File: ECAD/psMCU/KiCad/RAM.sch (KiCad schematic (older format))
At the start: 34 parts, among them U54 SN74LVC1G04DCK, U55 SN74LVC1G08DCK, U56 SN74LVC1G08DCK, U57 SN74LVC1G08DCK, U58 SN74LVC1G32DCK, U59 SN74LVC1G175DCK, U60 SN74LVC1G04DCK, U61 SN74LVC1G175DCK, U62 SN74LVC1G126DCK, U63 IS62C256AL-45T, U64 SN74LVC1G04DCK, U65 SN74LVC1G04DCK, U66 SN74HC245PW, U67 SN74HC245PW

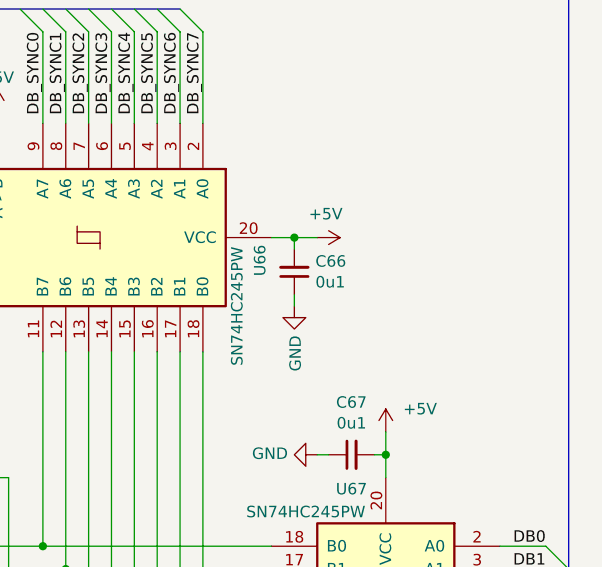
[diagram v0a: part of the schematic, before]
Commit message: Sch: Removed Regulator, Added extra spread bulk C
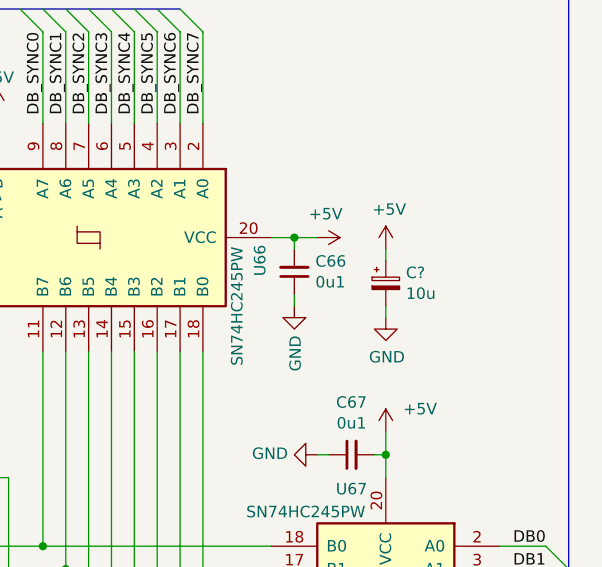
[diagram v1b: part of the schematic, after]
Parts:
- added C?: 10u, symbol Device:CP_Small
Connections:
- net +5V: now also C?.1
- net GND: now also C?.2
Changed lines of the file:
@@
 F9 "Latch_A" I L 3800 1600 50
 $EndSheet
+$Comp
+L Device:CP_Small C?
+U 1 1 625715F0
+P 9950 2000
+AR Path="/62043340/625715F0" Ref="C?"  Part="1"
+AR Path="/5FD6B215/625715F0" Ref="C?"  Part="1"
+F 0 "C?" H 10038 2046 50  0000 L CNN
+F 1 "10u" H 10038 1955 50  0000 L CNN
+F 2 "" H 9950 2000 50  0001 C CNN
+F 3 "~" H 9950 2000 50  0001 C CNN
+	1    9950 2000
+	1    0    0    -1
+$EndComp
+$Comp
+L power:GND #PWR?
+U 1 1 625715F6
+P 9950 2150
+AR Path="/625715F6" Ref="#PWR?"  Part="1"
+AR Path="/62043340/625715F6" Ref="#PWR?"  Part="1"
+AR Path="/5FD6B215/625715F6" Ref="#PWR?"  Part="1"
+F 0 "#PWR?" H 9950 1900 50  0001 C CNN
+F 1 "GND" H 9955 1977 50  0000 C CNN
+F 2 "" H 9950 2150 50  0001 C CNN
+F 3 "" H 9950 2150 50  0001 C CNN
+	1    9950 2150
+	1    0    0    -1
+$EndComp
+Wire Wire Line
+	9950 2150 9950 2100
+Wire Wire Line
+	9950 1850 9950 1900
+$Comp
+L power:+5V #PWR?
+U 1 1 625715FE
+P 9950 1850
+AR Path="/625715FE" Ref="#PWR?"  Part="1"
+AR Path="/62043340/625715FE" Ref="#PWR?"  Part="1"
+AR Path="/5FD6B215/625715FE" Ref="#PWR?"  Part="1"
+F 0 "#PWR?" H 9950 1700 50  0001 C CNN
+F 1 "+5V" H 9965 2023 50  0000 C CNN
+F 2 "" H 9950 1850 50  0001 C CNN
+F 3 "" H 9950 1850 50  0001 C CNN
+	1    9950 1850
+	1    0    0    -1
+$EndComp
 Wire Bus Line
 	5850 3350 5850 4000

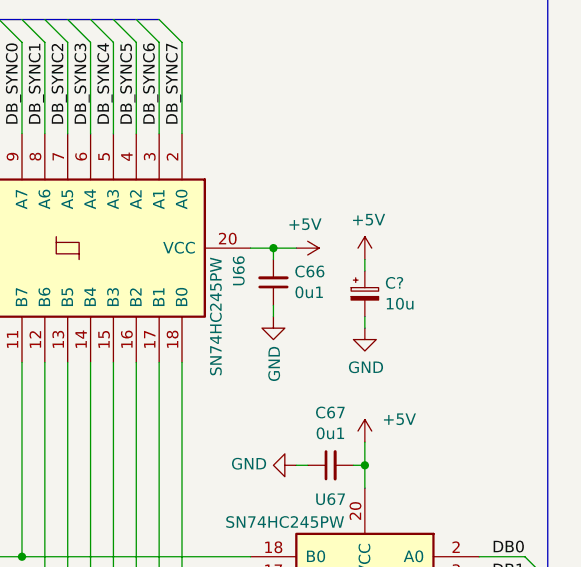
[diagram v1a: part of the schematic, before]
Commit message: Sch: Reworked Peripheral Interface (Buffers)
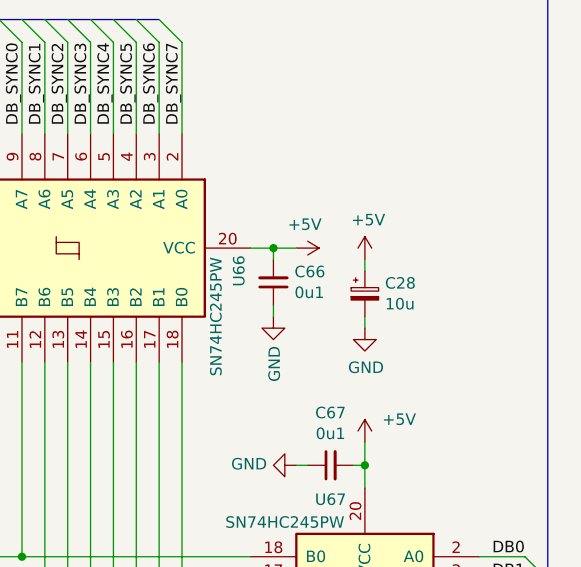
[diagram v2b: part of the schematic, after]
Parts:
- gave numbers to parts that had none: 1
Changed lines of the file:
@@
 $Descr A4 11693 8268
 encoding utf-8
-Sheet 34 97
+Sheet 34 96
 Title "psMCU"
 Date "2022-02-13"
@@
 AR Path="/62043340/625715F0" Ref="C?"  Part="1"
 AR Path="/5FD6B215/625715F0" Ref="C?"  Part="1"
-F 0 "C?" H 10038 2046 50  0000 L CNN
+AR Path="/5ED3C49A/625715F0" Ref="C28"  Part="1"
+F 0 "C28" H 10038 2046 50  0000 L CNN
 F 1 "10u" H 10038 1955 50  0000 L CNN
 F 2 "" H 9950 2000 50  0001 C CNN
@@
 AR Path="/62043340/625715F6" Ref="#PWR?"  Part="1"
 AR Path="/5FD6B215/625715F6" Ref="#PWR?"  Part="1"
-F 0 "#PWR?" H 9950 1900 50  0001 C CNN
+AR Path="/5ED3C49A/625715F6" Ref="#PWR0129"  Part="1"
+F 0 "#PWR0129" H 9950 1900 50  0001 C CNN
 F 1 "GND" H 9955 1977 50  0000 C CNN
 F 2 "" H 9950 2150 50  0001 C CNN
@@
 AR Path="/62043340/625715FE" Ref="#PWR?"  Part="1"
 AR Path="/5FD6B215/625715FE" Ref="#PWR?"  Part="1"
-F 0 "#PWR?" H 9950 1700 50  0001 C CNN
+AR Path="/5ED3C49A/625715FE" Ref="#PWR0130"  Part="1"
+F 0 "#PWR0130" H 9950 1700 50  0001 C CNN
 F 1 "+5V" H 9965 2023 50  0000 C CNN
 F 2 "" H 9950 1850 50  0001 C CNN

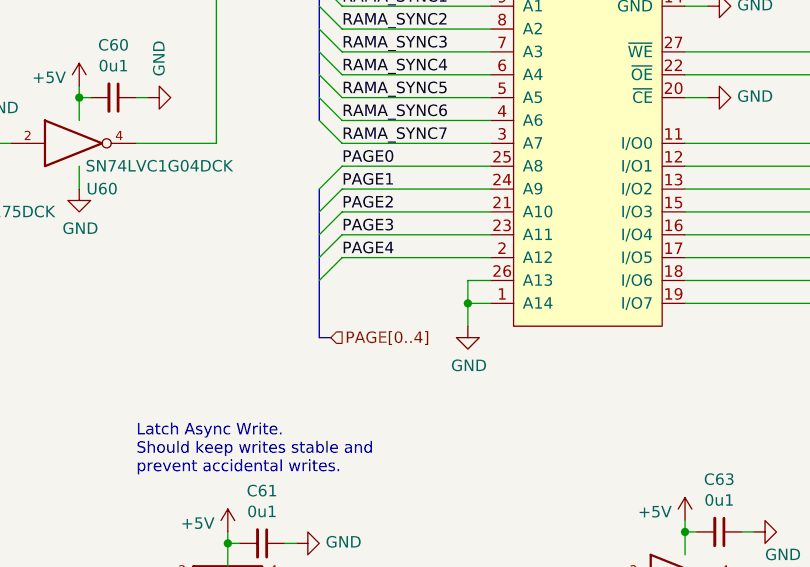
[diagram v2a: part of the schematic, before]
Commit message: Sch: Increased RAM page count, changed SYS registers
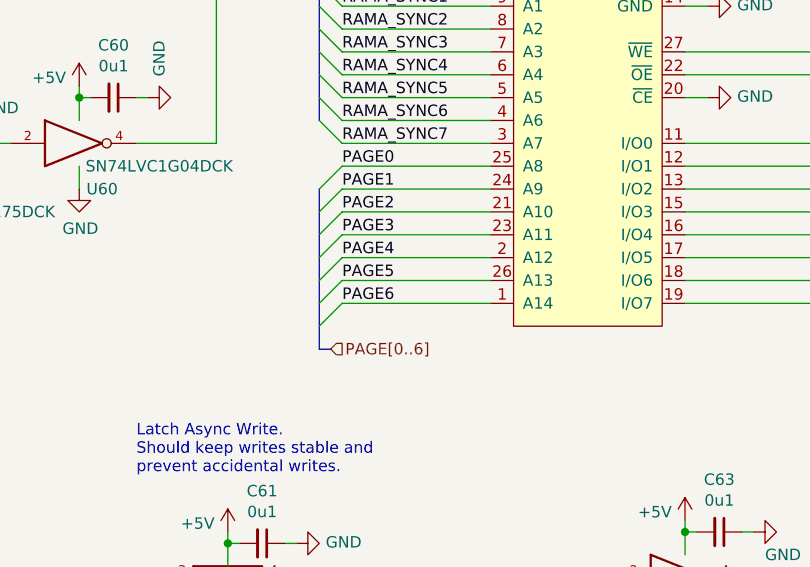
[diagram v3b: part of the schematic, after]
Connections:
- net GND: no longer U63.1 (A14), U63.26 (A13)
- new net PAGE5: U63.26 (A13)
- new net PAGE6: U63.1 (A14)
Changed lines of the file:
@@
 Entry Wire Line
 	5850 3050 5950 3150
-Wire Wire Line
-	6500 3850 6600 3850
-Wire Wire Line
-	6600 3750 6500 3750
-Wire Wire Line
-	6500 3750 6500 3850
-Wire Wire Line
-	6500 3850 6500 3950
-Connection ~ 6500 3850
-$Comp
-L power:GND #PWR0240
-U 1 1 5EF9BF8C
-P 6500 3950
-F 0 "#PWR0240" H 6500 3700 50  0001 C CNN
-F 1 "GND" H 6505 3777 50  0000 C CNN
-F 2 "" H 6500 3950 50  0001 C CNN
-F 3 "" H 6500 3950 50  0001 C CNN
-	1    6500 3950
-	1    0    0    -1
-$EndComp
 Wire Bus Line
 	5850 1400 5050 1400
@@
 Entry Wire Line
 	5950 3550 5850 3650
-Text HLabel 5900 4000 2    50   Input ~ 0
-PAGE[0..4]
+Text HLabel 5900 4050 2    50   Input ~ 0
+PAGE[0..6]
 Wire Bus Line
-	5850 4000 5900 4000
+	5850 4050 5900 4050
 Text HLabel 6150 6500 2    50   3State ~ 0
 DB_OUT
@@
 	1    0    0    -1
 $EndComp
+Text Label 5950 3750 0    50   ~ 0
+PAGE5
+Wire Wire Line
+	5950 3750 6600 3750
+Text Label 5950 3850 0    50   ~ 0
+PAGE6
+Wire Wire Line
+	5950 3850 6600 3850
+Entry Wire Line
+	5950 3750 5850 3850
+Entry Wire Line
+	5950 3850 5850 3950
 Wire Bus Line
-	5850 3350 5850 4000
+	5850 3350 5850 4050
 Wire Bus Line
 	6050 800  9050 800

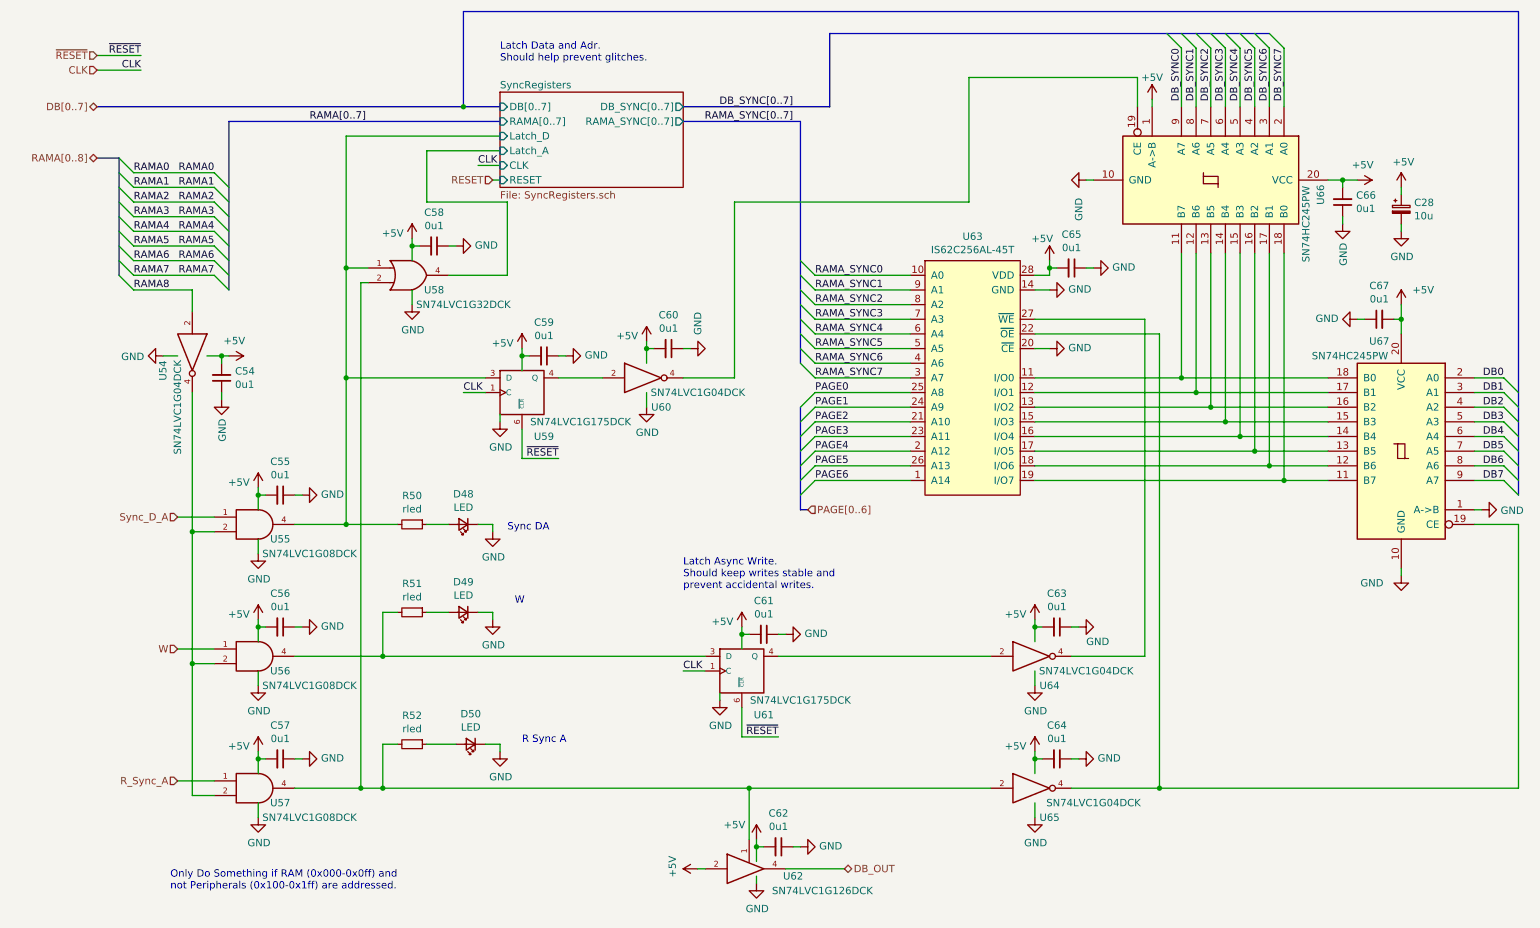
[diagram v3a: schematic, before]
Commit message: Sch: Improved Clk/Reset distribution, moved to global labels
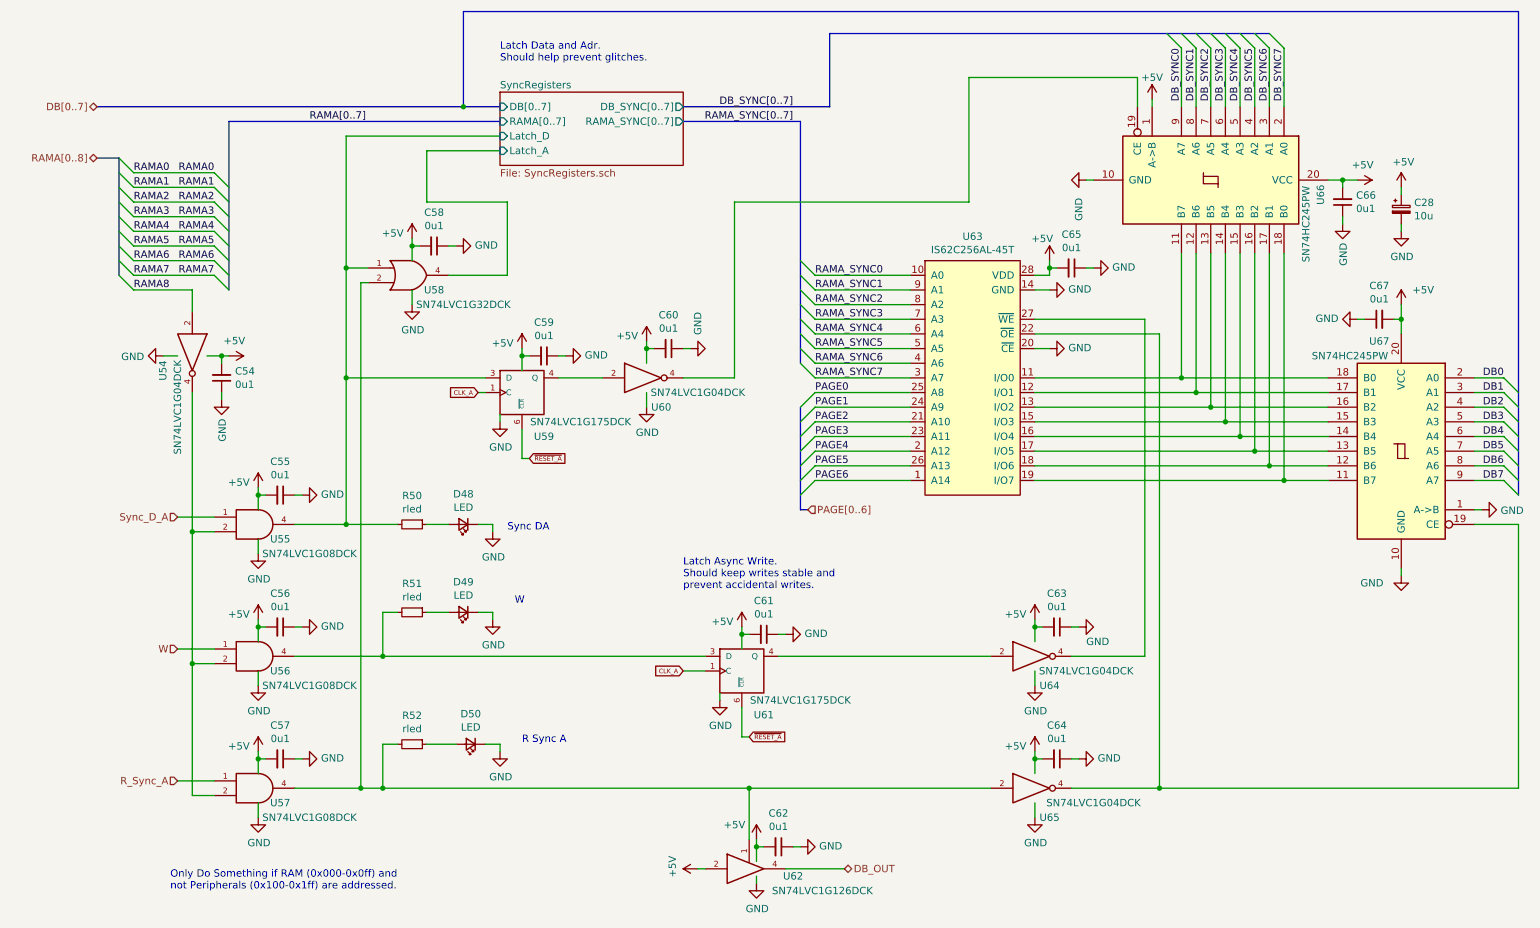
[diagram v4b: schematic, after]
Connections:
- net CLK renamed CLK_A
- net ~RESET renamed ~RESET_A
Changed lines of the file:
@@
 $Descr A4 11693 8268
 encoding utf-8
-Sheet 34 96
+Sheet 32 97
 Title "psMCU"
 Date "2022-02-13"
@@
 Text Label 1300 2550 0    50   ~ 0
 RAMA8
-Text HLabel 1050 1050 0    50   Input ~ 0
-CLK
-Wire Wire Line
-	1050 1050 1350 1050
-Text Label 1350 1050 2    50   ~ 0
-CLK
-Wire Wire Line
-	3800 1700 3650 1700
-Text Label 3650 1700 0    50   ~ 0
-CLK
 Wire Wire Line
 	1300 2550 1700 2550
@@
 Wire Wire Line
 	4250 3000 4200 3000
-Wire Wire Line
-	3700 3250 3550 3250
-Text Label 3550 3250 0    50   ~ 0
-CLK
 Entry Wire Line
 	5850 2350 5950 2450
@@
 Text Label 5800 1300 2    50   ~ 0
 DB_SYNC[0..7]
-Text HLabel 3750 1800 0    50   Input ~ 0
-RESET
-Wire Wire Line
-	3750 1800 3800 1800
 $Comp
 L 74xGxx:74LVC1G175 U61
@@
 Wire Wire Line
 	5200 5150 5050 5150
-Text Label 5050 5150 0    50   ~ 0
-CLK
 Wire Wire Line
 	5700 5050 7150 5050
@@
 	3000 5050 5200 5050
 Connection ~ 3000 5050
-Text HLabel 1050 950  0    50   Input ~ 0
-~RESET
 Wire Wire Line
 	5450 5400 5450 5600
@@
 	5500 5950 7150 5950
 Wire Wire Line
-	1050 950  1350 950
-Text Label 1350 950  2    50   ~ 0
-~RESET
-Text Label 4200 3700 2    50   ~ 0
-~RESET
-Text Label 5700 5600 2    50   ~ 0
-~RESET
-Wire Wire Line
-	5700 5600 5450 5600
-Wire Wire Line
-	4200 3700 3950 3700
-Wire Wire Line
 	3950 3500 3950 3700
 Connection ~ 2750 2400
@@
 R Sync A
 $Sheet
-S 3800 1200 1250 650
+S 3800 1200 1250 500
 U 5ED3C508
 F0 "SyncRegisters" 50
@@
 F2 "DB[0..7]" I L 3800 1300 50
 F3 "DB_SYNC[0..7]" O R 5050 1300 50
-F4 "CLK" I L 3800 1700 50
 F5 "RAMA[0..7]" I L 3800 1400 50
 F6 "RAMA_SYNC[0..7]" O R 5050 1400 50
-F7 "RESET" I L 3800 1800 50
 F8 "Latch_D" I L 3800 1500 50
 F9 "Latch_A" I L 3800 1600 50
@@
 Entry Wire Line
 	5950 3850 5850 3950
+Text GLabel 4000 3700 2    31   Input ~ 0
+~RESET_A
+Text GLabel 3650 3250 0    31   Input ~ 0
+CLK_A
+Wire Wire Line
+	3650 3250 3700 3250
+Wire Wire Line
+	4000 3700 3950 3700
+Text GLabel 5500 5600 2    31   Input ~ 0
+~RESET_A
+Text GLabel 5050 5150 0    31   Input ~ 0
+CLK_A
+Wire Wire Line
+	5500 5600 5450 5600
 Wire Bus Line
 	5850 3350 5850 4050
